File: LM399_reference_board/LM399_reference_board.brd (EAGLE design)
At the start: 42.5 x 42.5 mm, 1 part

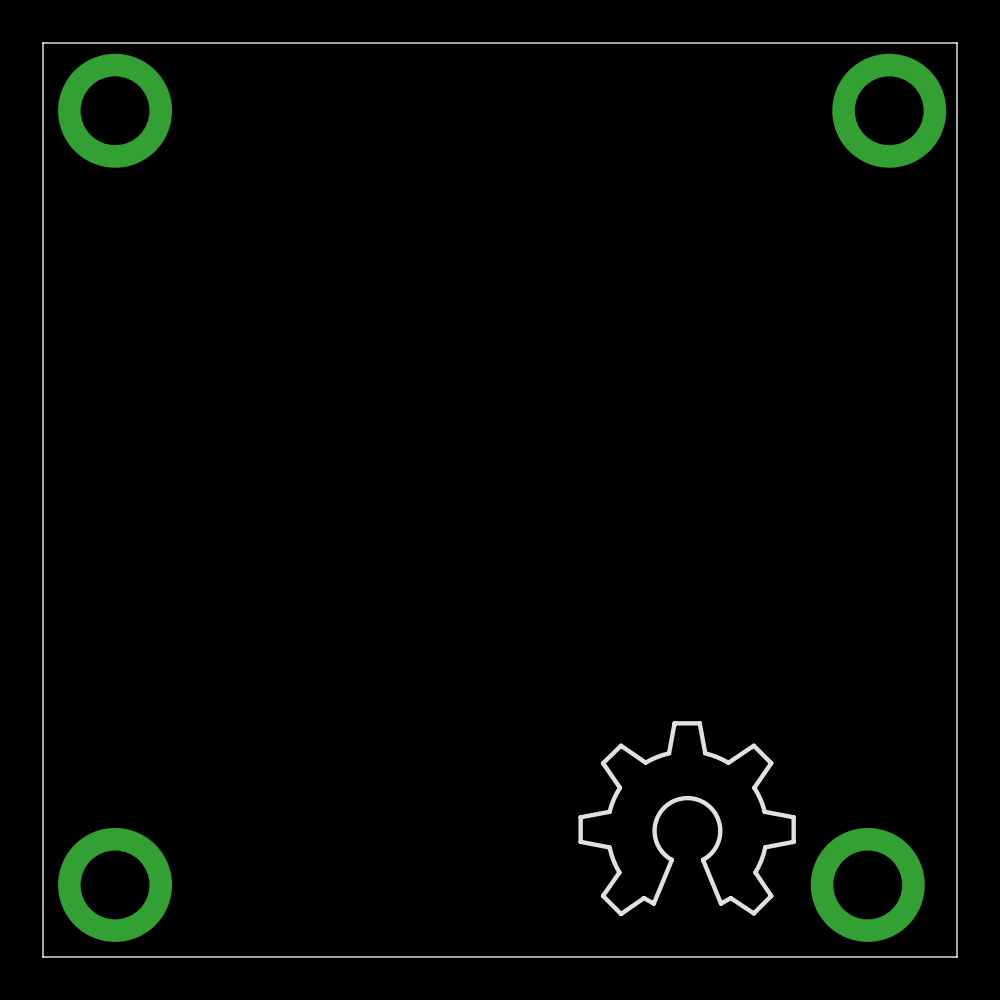
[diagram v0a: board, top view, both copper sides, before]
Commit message: * added start of the lm399 reference
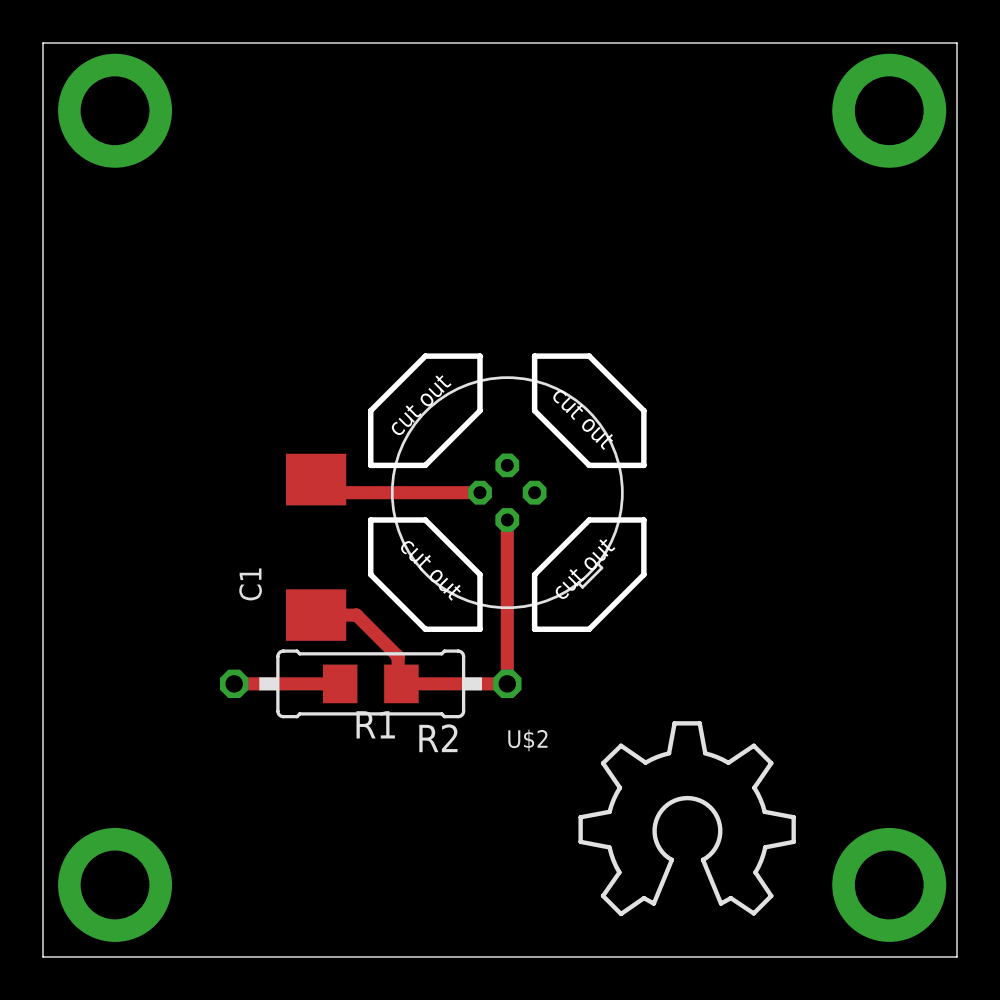
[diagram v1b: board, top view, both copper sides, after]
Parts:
- added C1: 10u, SquantorRCL:SMC_D
- added R1: (no value), SquantorRCL:R1206
- added R2: (no value), SquantorRCL:0309/12
- added U$2: LM399, SquantorLinearTechnology:H4-TO46-4PIN
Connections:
- new net +15V: R1.2, R2.2
- new net GND: C1.-, U$2.2, U$2.3
- new net N$5: C1.+, R1.1, R2.1, U$2.4
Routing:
- net N$5: track 0.00 -> 18.5 mm
- net GND: track 0.00 -> 7.87 mm
- net +15V: track 0.00 -> 4.93 mm
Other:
- outline, holes or cut-outs redrawn
- board text added: "cut out"
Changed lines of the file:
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@@
 <setting verticaltext="up"/>
 </settings>
-<grid distance="1" unitdist="mm" unit="mm" style="lines" multiple="1" display="yes" altdistance="0.025" altunitdist="inch" altunit="inch"/>
+<grid distance="1.27" unitdist="mm" unit="mm" style="lines" multiple="1" display="yes" altdistance="0.025" altunitdist="inch" altunit="inch"/>
 <layers>
 <layer number="1" name="Top" color="4" fill="1" visible="yes" active="yes"/>
@@
 <layer number="97" name="Info" color="7" fill="1" visible="no" active="no"/>
 <layer number="98" name="Guide" color="6" fill="1" visible="no" active="no"/>
+<layer number="99" name="SpiceOrder" color="5" fill="1" visible="no" active="no"/>
 <layer number="100" name="Muster" color="7" fill="1" visible="no" active="no"/>
 <layer number="101" name="DRAWREF" color="11" fill="1" visible="no" active="yes"/>
@@
 <layer number="106" name="bPlate" color="7" fill="1" visible="yes" active="yes"/>
 <layer number="107" name="Crop" color="7" fill="1" visible="yes" active="yes"/>
+<layer number="108" name="tBridges" color="7" fill="1" visible="yes" active="yes"/>
+<layer number="109" name="tBPL" color="7" fill="1" visible="yes" active="yes"/>
+<layer number="110" name="bBPL" color="7" fill="1" visible="yes" active="yes"/>
+<layer number="111" name="MPL" color="7" fill="1" visible="yes" active="yes"/>
+<layer number="112" name="tSilk" color="7" fill="1" visible="yes" active="yes"/>
 <layer number="116" name="Patch_BOT" color="9" fill="4" visible="yes" active="yes"/>
 <layer number="121" name="_tsilk" color="7" fill="1" visible="yes" active="yes"/>
 <layer number="122" name="_bsilk" color="7" fill="1" visible="yes" active="yes"/>
+<layer number="125" name="_tNames" color="7" fill="1" visible="yes" active="yes"/>
+<layer number="126" name="_bNames" color="7" fill="1" visible="yes" active="yes"/>
+<layer number="127" name="_tValues" color="7" fill="1" visible="yes" active="yes"/>
+<layer number="128" name="_bValues" color="7" fill="1" visible="yes" active="yes"/>
 <layer number="144" name="DrillLegend" color="7" fill="1" visible="no" active="yes"/>
 <layer number="151" name="HeatSink" color="7" fill="1" visible="yes" active="yes"/>
+<layer number="152" name="_bDocu" color="7" fill="1" visible="yes" active="yes"/>
 <layer number="200" name="200bmp" color="1" fill="10" visible="no" active="yes"/>
 <layer number="201" name="201bmp" color="2" fill="10" visible="no" active="yes"/>
@@
 <layer number="215" name="215bmp" color="7" fill="1" visible="yes" active="yes"/>
 <layer number="216" name="216bmp" color="7" fill="1" visible="yes" active="yes"/>
+<layer number="248" name="Housing" color="7" fill="1" visible="yes" active="yes"/>
+<layer number="249" name="Edge" color="7" fill="1" visible="yes" active="yes"/>
 <layer number="250" name="Descript" color="3" fill="1" visible="no" active="no"/>
 <layer number="251" name="SMDround" color="12" fill="11" visible="no" active="no"/>
@@
 <wire x1="42.5" y1="42.5" x2="0" y2="42.5" width="0" layer="20"/>
 <wire x1="0" y1="42.5" x2="0" y2="0" width="0" layer="20"/>
+<wire x1="17.78" y1="22.86" x2="20.32" y2="25.4" width="0.254" layer="20"/>
+<wire x1="20.32" y1="25.4" x2="20.32" y2="27.94" width="0.254" layer="20"/>
+<wire x1="20.32" y1="27.94" x2="17.78" y2="27.94" width="0.254" layer="20"/>
+<wire x1="17.78" y1="27.94" x2="15.24" y2="25.4" width="0.254" layer="20"/>
+<wire x1="15.24" y1="25.4" x2="15.24" y2="22.86" width="0.254" layer="20"/>
+<wire x1="15.24" y1="22.86" x2="17.78" y2="22.86" width="0.254" layer="20"/>
+<wire x1="22.86" y1="27.94" x2="22.86" y2="25.4" width="0.254" layer="20"/>
+<wire x1="22.86" y1="25.4" x2="25.4" y2="22.86" width="0.254" layer="20"/>
+<wire x1="25.4" y1="22.86" x2="27.94" y2="22.86" width="0.254" layer="20"/>
+<wire x1="27.94" y1="22.86" x2="27.94" y2="25.4" width="0.254" layer="20"/>
+<wire x1="27.94" y1="25.4" x2="25.4" y2="27.94" width="0.254" layer="20"/>
+<wire x1="25.4" y1="27.94" x2="22.86" y2="27.94" width="0.254" layer="20"/>
+<wire x1="25.4" y1="20.32" x2="27.94" y2="20.32" width="0.254" layer="20"/>
+<wire x1="27.94" y1="20.32" x2="27.94" y2="17.78" width="0.254" layer="20"/>
+<wire x1="27.94" y1="17.78" x2="25.4" y2="15.24" width="0.254" layer="20"/>
+<wire x1="25.4" y1="15.24" x2="22.86" y2="15.24" width="0.254" layer="20"/>
+<wire x1="22.86" y1="15.24" x2="22.86" y2="17.78" width="0.254" layer="20"/>
+<wire x1="22.86" y1="17.78" x2="25.4" y2="20.32" width="0.254" layer="20"/>
+<wire x1="15.24" y1="20.32" x2="17.78" y2="20.32" width="0.254" layer="20"/>
+<wire x1="17.78" y1="20.32" x2="20.32" y2="17.78" width="0.254" layer="20"/>
+<wire x1="20.32" y1="17.78" x2="20.32" y2="15.24" width="0.254" layer="20"/>
+<wire x1="20.32" y1="15.24" x2="17.78" y2="15.24" width="0.254" layer="20"/>
+<wire x1="17.78" y1="15.24" x2="15.24" y2="17.78" width="0.254" layer="20"/>
+<wire x1="15.24" y1="17.78" x2="15.24" y2="20.32" width="0.254" layer="20"/>
+<text x="16.51" y="24.13" size="0.8128" layer="20" rot="R45">cut out</text>
+<text x="26.67" y="24.13" size="0.8128" layer="20" rot="R135">cut out</text>
+<text x="24.13" y="16.51" size="0.8128" layer="20" rot="R45">cut out</text>
+<text x="16.51" y="19.05" size="0.8128" layer="20" rot="R315">cut out</text>
 </plain>
 <attributes>
@@
 <elements>
 <element name="U$1" library="ohw-logo" package="OSHW_8X350_NOTEXT" value="" x="25" y="2"/>
+<element name="U$2" library="SquantorLinearTechnology" package="H4-TO46-4PIN" value="LM399" x="21.59" y="21.59" rot="R180"/>
+<element name="C1" library="SquantorRCL" package="SMC_D" value="10u" x="12.7" y="19.05" rot="R90"/>
+<element name="R1" library="SquantorRCL" package="R1206" value="" x="15.24" y="12.7" rot="R180"/>
+<element name="R2" library="SquantorRCL" package="0309/12" value="" x="15.24" y="12.7" rot="R180"/>
 </elements>
 <signals>
@@
 </signal>
 <signal name="N$2">
-<via x="38.35" y="3.35" extent="1-16" drill="3.2" diameter="5.3"/>
+<via x="39.35" y="3.35" extent="1-16" drill="3.2" diameter="5.3"/>
 </signal>
 <signal name="N$3">
@@
 <via x="3.35" y="39.35" extent="1-16" drill="3.2" diameter="5.3"/>
 </signal>
+<signal name="GND">
+<contactref element="U$2" pad="3"/>
+<contactref element="U$2" pad="2"/>
+<contactref element="C1" pad="-"/>
+<wire x1="20.32" y1="21.59" x2="21.59" y2="22.86" width="0" layer="19" extent="1-1"/>
+<wire x1="20.32" y1="21.59" x2="13.31" y2="21.59" width="0.6096" layer="1"/>
+<wire x1="13.31" y1="21.59" x2="12.7" y2="22.2" width="0.6096" layer="1"/>
+</signal>
+<signal name="N$5">
+<contactref element="C1" pad="+"/>
+<contactref element="U$2" pad="4"/>
+<contactref element="R2" pad="1"/>
+<contactref element="R1" pad="1"/>
+<wire x1="12.7" y1="15.9" x2="14.58" y2="15.9" width="0.6096" layer="1"/>
+<wire x1="14.58" y1="15.9" x2="16.51" y2="13.97" width="0.6096" layer="1"/>
+<wire x1="16.51" y1="13.97" x2="16.51" y2="12.852" width="0.6096" layer="1"/>
+<wire x1="16.51" y1="12.852" x2="16.662" y2="12.7" width="0.6096" layer="1"/>
+<wire x1="16.662" y1="12.7" x2="21.59" y2="12.7" width="0.6096" layer="1"/>
+<wire x1="21.59" y1="12.7" x2="21.59" y2="20.32" width="0.6096" layer="1"/>
+</signal>
+<signal name="+15V">
+<contactref element="R1" pad="2"/>
+<contactref element="R2" pad="2"/>
+<wire x1="8.89" y1="12.7" x2="13.818" y2="12.7" width="0.6096" layer="1"/>
+</signal>
 </signals>

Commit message: * Additional work with LM399
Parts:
- added C2: 100n, SquantorRCL:C0603
- added C3: 10u, SquantorRCL:SMC_D
- added R3: 220k, SquantorRCL:0207/10
- added R4: 5k, SquantorRCL:0207/10
- added R5: 8.8k, SquantorRCL:0207/10
- added R6: 19k, SquantorRCL:0207/10
- added R7: (no value), SquantorRCL:RTRIMT93YA
- added U$3: LTC2057, SquantorLinearTechnology:MS-MSOP10
- R1, R2: value (none) -> inrush
- moved U$1 8.98 mm to (16.1, 0.73)
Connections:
- new net N$6: R5.1, R6.2, U$3.1, U$3.2, U$3.4
- new net N$7: R4.1, R5.2, U$3.6
- new net N$8: R6.1, R7.1
- new net VZENER: R3.1, R4.2, U$2.1, U$3.3
- net +15V: now also C2.2, C3.+, R3.2, U$3.8
- net GND: now also C2.1, C3.-, R7.2, R7.3, U$3.5
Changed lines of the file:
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@@
 </autorouter>
 <elements>
-<element name="U$1" library="ohw-logo" package="OSHW_8X350_NOTEXT" value="" x="25" y="2"/>
+<element name="U$1" library="ohw-logo" package="OSHW_8X350_NOTEXT" value="" x="16.11" y="0.73"/>
 <element name="U$2" library="SquantorLinearTechnology" package="H4-TO46-4PIN" value="LM399" x="21.59" y="21.59" rot="R180"/>
 <element name="C1" library="SquantorRCL" package="SMC_D" value="10u" x="12.7" y="19.05" rot="R90"/>
-<element name="R1" library="SquantorRCL" package="R1206" value="" x="15.24" y="12.7" rot="R180"/>
-<element name="R2" library="SquantorRCL" package="0309/12" value="" x="15.24" y="12.7" rot="R180"/>
+<element name="R1" library="SquantorRCL" package="R1206" value="inrush" x="15.24" y="12.7" rot="R180"/>
+<element name="R2" library="SquantorRCL" package="0309/12" value="inrush" x="15.24" y="12.7" rot="R180"/>
+<element name="U$3" library="SquantorLinearTechnology" package="MS-MSOP10" value="LTC2057" x="21.59" y="33.02" rot="R90"/>
+<element name="R3" library="SquantorRCL" package="0207/10" value="220k" x="30.48" y="16.51" rot="R270"/>
+<element name="R4" library="SquantorRCL" package="0207/10" value="5k" x="30.48" y="29.21" rot="R270"/>
+<element name="R5" library="SquantorRCL" package="0207/10" value="8.8k" x="17.78" y="34.29" rot="R90"/>
+<element name="R6" library="SquantorRCL" package="0207/10" value="19k" x="13.97" y="34.29" rot="R270"/>
+<element name="R7" library="SquantorRCL" package="RTRIMT93YA" value="" x="8.89" y="34.29" rot="R180"/>
+<element name="C2" library="SquantorRCL" package="C0603" value="100n" x="26.67" y="33.02" rot="R90"/>
+<element name="C3" library="SquantorRCL" package="SMC_D" value="10u" x="38.1" y="30.48" rot="R270"/>
 </elements>
 <signals>
@@
 <contactref element="U$2" pad="2"/>
 <contactref element="C1" pad="-"/>
-<wire x1="20.32" y1="21.59" x2="21.59" y2="22.86" width="0" layer="19" extent="1-1"/>
 <wire x1="20.32" y1="21.59" x2="13.31" y2="21.59" width="0.6096" layer="1"/>
 <wire x1="13.31" y1="21.59" x2="12.7" y2="22.2" width="0.6096" layer="1"/>
+<contactref element="U$3" pad="5"/>
+<contactref element="R7" pad="3"/>
+<contactref element="R7" pad="2"/>
+<contactref element="C2" pad="1"/>
+<contactref element="C3" pad="-"/>
+<wire x1="26.67" y1="32.17" x2="38.1" y2="27.33" width="0" layer="19" extent="1-1"/>
+<wire x1="22.59" y1="30.845" x2="26.67" y2="32.17" width="0" layer="19" extent="1-1"/>
+<wire x1="21.59" y1="22.86" x2="22.59" y2="30.845" width="0" layer="19" extent="1-1"/>
+<wire x1="20.32" y1="21.59" x2="21.59" y2="22.86" width="0" layer="19" extent="1-1"/>
+<wire x1="8.89" y1="31.75" x2="12.7" y2="22.2" width="0" layer="19" extent="1-1"/>
+<wire x1="8.89" y1="34.29" x2="8.89" y2="31.75" width="0" layer="19" extent="1-1"/>
 </signal>
 <signal name="N$5">
@@
 <contactref element="R2" pad="2"/>
 <wire x1="8.89" y1="12.7" x2="13.818" y2="12.7" width="0.6096" layer="1"/>
+<contactref element="R3" pad="2"/>
+<contactref element="U$3" pad="8"/>
+<contactref element="C2" pad="2"/>
+<contactref element="C3" pad="+"/>
+<wire x1="26.67" y1="33.87" x2="38.1" y2="33.63" width="0" layer="19" extent="1-1"/>
+<wire x1="21.59" y1="35.195" x2="26.67" y2="33.87" width="0" layer="19" extent="1-1"/>
+<wire x1="30.48" y1="11.43" x2="26.67" y2="33.87" width="0" layer="19" extent="1-1"/>
+<wire x1="13.818" y1="12.7" x2="30.48" y2="11.43" width="0" layer="19" extent="1-1"/>
+</signal>
+<signal name="VZENER">
+<contactref element="R3" pad="1"/>
+<contactref element="U$2" pad="1"/>
+<contactref element="U$3" pad="3"/>
+<contactref element="R4" pad="2"/>
+<wire x1="30.48" y1="21.59" x2="30.48" y2="24.13" width="0" layer="19" extent="1-1"/>
+<wire x1="22.86" y1="21.59" x2="30.48" y2="21.59" width="0" layer="19" extent="1-1"/>
+<wire x1="21.59" y1="30.845" x2="22.86" y2="21.59" width="0" layer="19" extent="1-1"/>
+</signal>
+<signal name="N$7">
+<contactref element="U$3" pad="6"/>
+<contactref element="R5" pad="2"/>
+<contactref element="R4" pad="1"/>
+<wire x1="22.59" y1="35.195" x2="30.48" y2="34.29" width="0" layer="19" extent="1-1"/>
+<wire x1="17.78" y1="39.37" x2="22.59" y2="35.195" width="0" layer="19" extent="1-1"/>
+</signal>
+<signal name="N$6">
+<contactref element="R5" pad="1"/>
+<contactref element="R6" pad="2"/>
+<contactref element="U$3" pad="2"/>
+<contactref element="U$3" pad="1"/>
+<contactref element="U$3" pad="4"/>
+<wire x1="20.59" y1="30.845" x2="21.09" y2="30.845" width="0" layer="19" extent="1-1"/>
+<wire x1="22.09" y1="30.845" x2="21.09" y2="30.845" width="0" layer="19" extent="1-1"/>
+<wire x1="17.78" y1="29.21" x2="20.59" y2="30.845" width="0" layer="19" extent="1-1"/>
+<wire x1="13.97" y1="29.21" x2="17.78" y2="29.21" width="0" layer="19" extent="1-1"/>
+</signal>
+<signal name="N$8">
+<contactref element="R6" pad="1"/>
+<contactref element="R7" pad="1"/>
+<wire x1="8.89" y1="36.83" x2="13.97" y2="39.37" width="0" layer="19" extent="1-1"/>
 </signal>
 </signals>
